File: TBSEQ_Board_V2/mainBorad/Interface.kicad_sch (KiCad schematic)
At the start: 48 parts, among them IC11 AN6562, IC12 4066, J7 Conn_01x03_Pin, J8 Conn_01x02_Pin, J9 Conn_01x01_Pin, Q29 NPN, Q30 NPN, Q35 NPN, Q36 PNP, Q37 NPN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

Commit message: mainboard
PWS,Digi
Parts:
- removed VR6: 1M(A), SamacSys_Parts:PTV1113420AA103, symbol SamacSys_Parts:PTV111-3420A-A103
- removed VR7: 50K(B), SamacSys_Parts:PTV1113420AA103, symbol SamacSys_Parts:PTV111-3420A-A103
- added VR_J_6, VR_J_7: Conn_01x03_Pin, Connector_PinHeader_2.54mm:PinHeader_1x03_P2.54mm_Vertical, symbol Connector:Conn_01x03_Pin
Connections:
- net A+VCA-Reso_ACC: now also VR_J_7.2 (Pin_2)
- net GNDA: now also VR_J_7.1 (Pin_1)
- net at IC12.8: now also VR_J_7.3 (Pin_3)
- net at D28.2 (A), IC12.10: now also VR_J_6.2 (Pin_2), VR_J_6.3 (Pin_3)
- net at IC12.11, R138.1: now also VR_J_6.1 (Pin_1)
- no-connect marks 2 -> 0
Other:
- note added: "CCW"
- note added: "CW"
- note added: "WIPER"

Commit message: mainBoard
AnInterface
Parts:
- removed VR_J_6, VR_J_7: Conn_01x03_Pin, Connector_PinHeader_2.54mm:PinHeader_1x03_P2.54mm_Vertical, symbol Connector:Conn_01x03_Pin
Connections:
- net A_VR6_CCW: now reaches IC12.11, R138.1
- net A_VR6_WIPER_CW: now reaches D28.2 (A), IC12.10
- net A_VR7_CW: now reaches IC12.8
- net D+GATE renamed A+GATE
- net D+SLIDE renamed A+SLIDE
- net D-ACC renamed A-ACC
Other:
- note added: "A_VR6_WIPERはCWと接続"
- note added: "A_VR7_CCWはGNDAと接続"
- note added: "AccentVolume"
- note removed: "CCW"
- note removed: "CW"
- note removed: "WIPER"

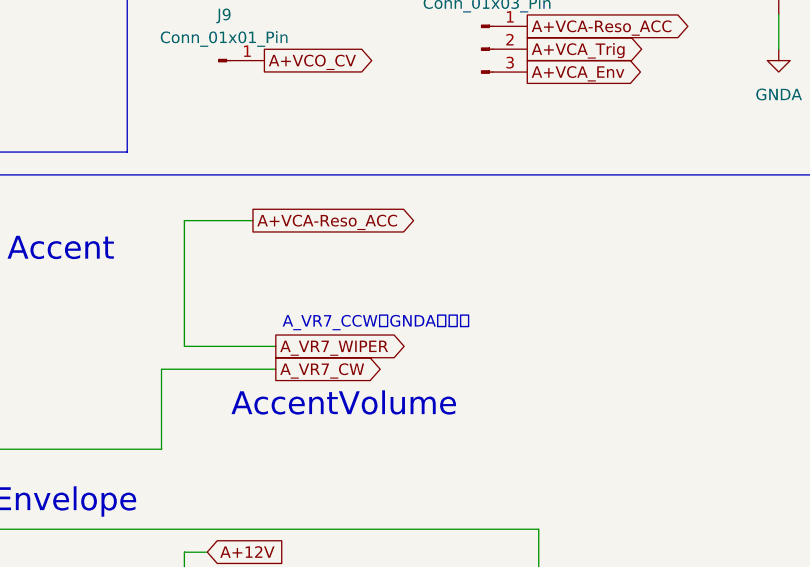
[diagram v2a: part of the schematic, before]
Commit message: mainboard
部品を全部配置しただけ
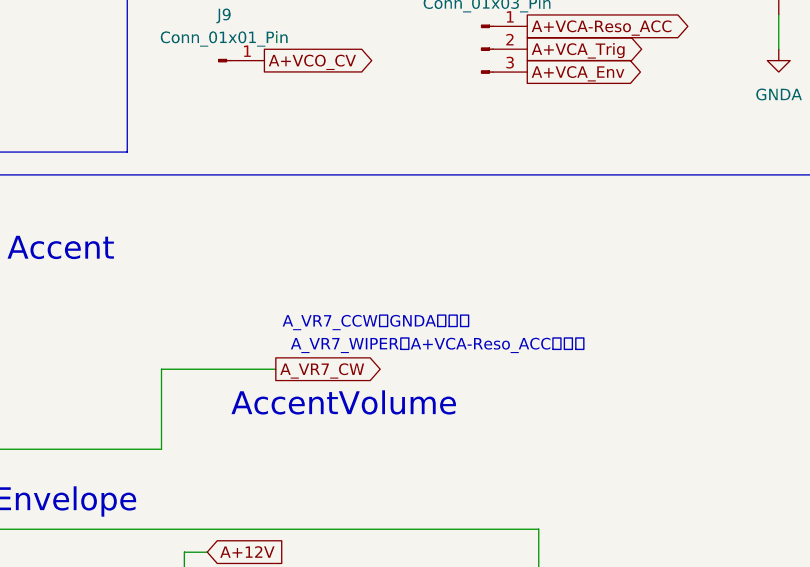
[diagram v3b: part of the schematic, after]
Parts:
- J7: footprint Connector_PinHeader_2.54mm:PinHeader_1x03_P2.54mm_Vertical -> Connector_PinHeader_2.54mm:PinHeader_1x03_P2.54mm_Horizontal
- J8: footprint Connector_PinHeader_2.54mm:PinHeader_1x02_P2.54mm_Vertical -> Connector_PinHeader_2.54mm:PinHeader_1x02_P2.54mm_Horizontal
- J9: footprint Connector_PinHeader_2.54mm:PinHeader_1x01_P2.54mm_Vertical -> Connector_PinHeader_2.54mm:PinHeader_1x01_P2.54mm_Horizontal
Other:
- note added: "A_VR7_WIPERはA+VCA-Reso_ACCと接続"
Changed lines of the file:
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@@
 	(wire
 		(pts
-			(xy 171.45 72.39) (xy 179.07 72.39)
-		)
-		(stroke
-			(width 0)
-			(type default)
-		)
-	)
-	(wire
-		(pts
 			(xy 179.07 125.73) (xy 179.07 133.35)
 		)
@@
 	(wire
 		(pts
-			(xy 181.61 86.36) (xy 171.45 86.36)
-		)
-		(stroke
-			(width 0)
-			(type default)
-		)
-	)
-	(wire
-		(pts
 			(xy 104.14 111.76) (xy 110.49 111.76)
 		)
@@
 	(wire
 		(pts
-			(xy 171.45 86.36) (xy 171.45 72.39)
-		)
-		(stroke
-			(width 0)
-			(type default)
-		)
-	)
-	(wire
-		(pts
 			(xy 60.96 55.88) (xy 64.77 55.88)
 		)
@@
 		)
 	)
+	(text "A_VR7_WIPERはA+VCA-Reso_ACCと接続"
+		(exclude_from_sim no)
+		(at 199.644 86.36 0)
+		(effects
+			(font
+				(size 1.27 1.27)
+			)
+		)
+	)
 	(text "TB303_V2では4558で置換"
 		(exclude_from_sim no)
@@
 		)
 	)
-	(global_label "A_VR7_WIPER"
-		(shape output)
-		(at 181.61 86.36 0)
-		(fields_autoplaced yes)
-		(effects
-			(font
-				(size 1.27 1.27)
-			)
-			(justify left)
-		)
-		(property "Intersheetrefs" "${INTERSHEET_REFS}"
-			(at 196.9323 86.36 0)
-			(effects
-				(font
-					(size 1.27 1.27)
-				)
-				(justify left)
-				(hide yes)
-			)
-		)
-	)
-	(global_label "A+VCA-Reso_ACC"
-		(shape output)
-		(at 179.07 72.39 0)
-		(fields_autoplaced yes)
-		(effects
-			(font
-				(size 1.27 1.27)
-			)
-			(justify left)
-		)
-		(property "Intersheetrefs" "${INTERSHEET_REFS}"
-			(at 197.2953 72.39 0)
-			(effects
-				(font
-					(size 1.27 1.27)
-				)
-				(justify left)
-				(hide yes)
-			)
-		)
-	)
 	(global_label "A+12V"
 		(shape input)
@@
 			)
 		)
-		(property "Footprint" "Connector_PinHeader_2.54mm:PinHeader_1x01_P2.54mm_Vertical"
+		(property "Footprint" "Connector_PinHeader_2.54mm:PinHeader_1x01_P2.54mm_Horizontal"
 			(at 175.26 54.61 0)
 			(effects
@@
 			)
 		)
-		(property "Footprint" "Connector_PinHeader_2.54mm:PinHeader_1x03_P2.54mm_Vertical"
+		(property "Footprint" "Connector_PinHeader_2.54mm:PinHeader_1x03_P2.54mm_Horizontal"
 			(at 204.47 53.34 0)
 			(effects
@@
 			)
 		)
-		(property "Footprint" "Connector_PinHeader_2.54mm:PinHeader_1x02_P2.54mm_Vertical"
+		(property "Footprint" "Connector_PinHeader_2.54mm:PinHeader_1x02_P2.54mm_Horizontal"
 			(at 201.93 26.67 0)
 			(effects
